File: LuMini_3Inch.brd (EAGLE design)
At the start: 76.2 x 76.2 mm, 97 parts, among them J1 SOLDER_PAD_2, J2 SOLDER_PAD_2, J3 SOLDER_PAD_2

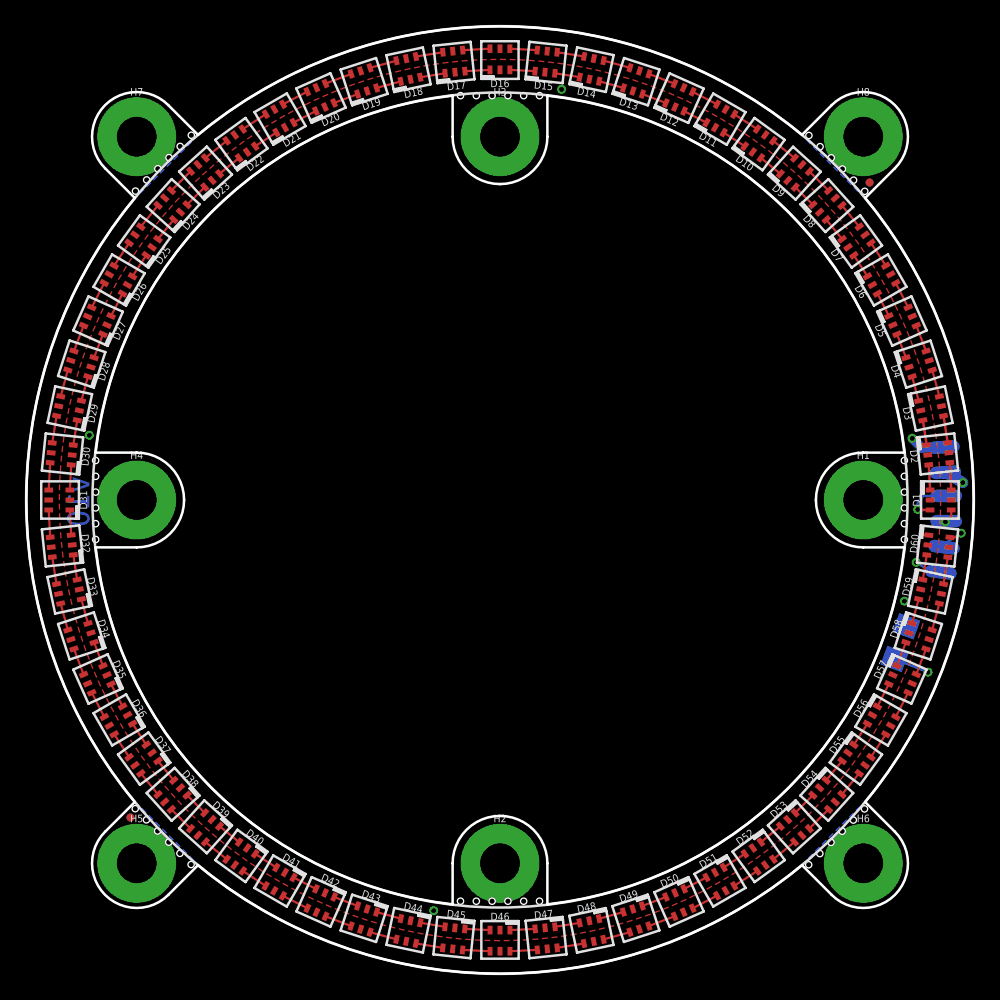
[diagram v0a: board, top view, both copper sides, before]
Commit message: added lumini ring
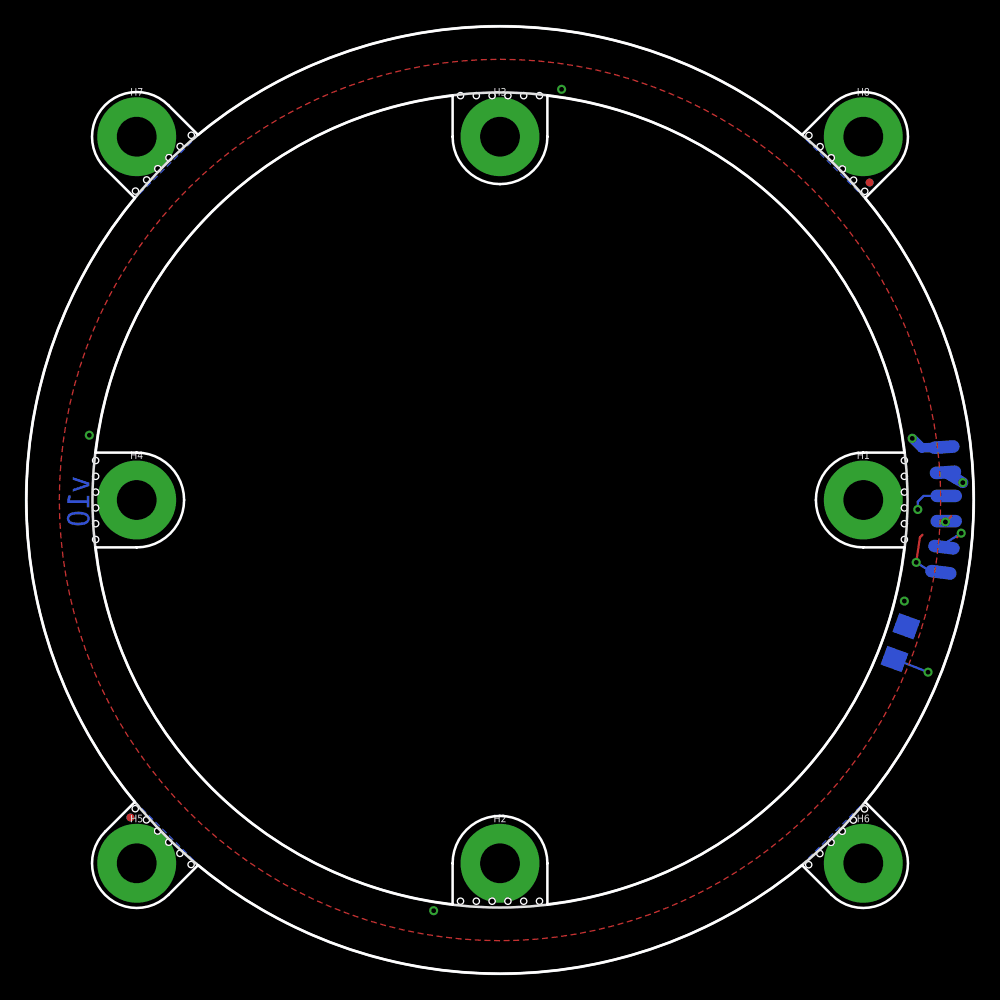
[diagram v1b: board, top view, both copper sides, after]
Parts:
- removed D1, D10, D11, D12, D13, D14, D15, D16, D17, D18, D19, D2, D20, D21, D22, D23, D24, D25, D26, D27, D28, D29, D3, D30, D31, D32, D33, D34, D35, D36, D37, D38, D39, D4, D40, D41, D42, D43, D44, D45, D46, D47, D48, D49, D5, D50, D51, D52, D53, D54, D55, D56, D57, D58, D59, D6, D60, D7, D8, D9: APA102-2020, SparkFun-LED:APA102-2020
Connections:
- removed net N$1: D4.CKO, D5.CKI
- removed net N$10: D4.SDO, D5.SDI
- removed net N$100: D50.CKO, D51.CKI
- removed net N$101: D50.SDO, D51.SDI
- removed net N$102: D51.CKO, D52.CKI
- removed net N$103: D51.SDO, D52.SDI
- removed net N$104: D52.CKO, D53.CKI
- removed net N$105: D52.SDO, D53.SDI
- removed net N$106: D53.CKO, D54.CKI
- removed net N$107: D53.SDO, D54.SDI
- removed net N$108: D54.CKO, D55.CKI
- removed net N$109: D54.SDO, D55.SDI
- removed net N$11: D5.CKO, D6.CKI
- removed net N$110: D55.CKO, D56.CKI
- removed net N$111: D55.SDO, D56.SDI
- removed net N$112: D57.CKO, D58.CKI
- removed net N$113: D57.SDO, D58.SDI
- removed net N$114: D58.SDO, D59.SDI
- removed net N$115: D59.CKO, D60.CKI
- removed net N$116: D59.SDO, D60.SDI
- removed net N$117: D58.CKO, D59.CKI
- removed net N$118: D48.CKO, D49.CKI
- removed net N$119: D48.SDO, D49.SDI
- removed net N$12: D5.SDO, D6.SDI
- removed net N$120: D56.SDO, D57.SDI
- removed net N$121: D56.CKO, D57.CKI
- removed net N$124: D20.CKO, D21.CKI
- removed net N$13: D6.CKO, D7.CKI
- removed net N$14: D6.SDO, D7.SDI
- removed net N$15: D7.CKO, D8.CKI
- removed net N$16: D7.SDO, D8.SDI
- removed net N$17: D16.SDO, D17.SDI
- removed net N$18: D20.SDO, D21.SDI
- removed net N$19: D10.CKI, D9.CKO
- removed net N$20: D10.SDI, D9.SDO
- removed net N$21: D10.CKO, D11.CKI
- removed net N$22: D10.SDO, D11.SDI
- removed net N$23: D11.CKO, D12.CKI
- removed net N$24: D11.SDO, D12.SDI
- removed net N$25: D12.CKO, D13.CKI
- removed net N$26: D12.SDO, D13.SDI
- removed net N$27: D13.CKO, D14.CKI
- removed net N$28: D13.SDO, D14.SDI
- removed net N$29: D14.CKO, D15.CKI
- removed net N$30: D14.SDO, D15.SDI
- removed net N$31: D45.CKO, D46.CKI
- removed net N$32: D30.CKO, D31.CKI
- removed net N$33: D8.CKO, D9.CKI
- removed net N$34: D8.SDO, D9.SDI
- removed net N$35: D17.CKO, D18.CKI
- removed net N$36: D17.SDO, D18.SDI
- removed net N$37: D18.CKO, D19.CKI
- removed net N$38: D18.SDO, D19.SDI
- removed net N$39: D19.CKO, D20.CKI
- removed net N$4: D1.CKO, D2.CKI
- removed net N$40: D19.SDO, D20.SDI
- removed net N$41: D30.SDO, D31.SDI
- removed net N$42: D15.CKO, D16.CKI
- removed net N$43: D16.CKO, D17.CKI
- removed net N$44: D21.CKO, D22.CKI
- removed net N$45: D21.SDO, D22.SDI
- removed net N$46: D22.CKO, D23.CKI
- removed net N$47: D22.SDO, D23.SDI
- removed net N$48: D23.CKO, D24.CKI
- removed net N$49: D23.SDO, D24.SDI
- removed net N$5: D1.SDO, D2.SDI
- removed net N$50: D24.CKO, D25.CKI
- removed net N$51: D24.SDO, D25.SDI
- removed net N$52: D25.CKO, D26.CKI
- removed net N$53: D25.SDO, D26.SDI
- removed net N$54: D26.CKO, D27.CKI
- removed net N$55: D26.SDO, D27.SDI
- removed net N$56: D27.CKO, D28.CKI
- removed net N$57: D27.SDO, D28.SDI
- removed net N$58: D29.CKO, D30.CKI
- removed net N$59: D29.SDO, D30.SDI
- removed net N$6: D2.CKO, D3.CKI
- removed net N$60: D15.SDO, D16.SDI
- removed net N$61: D45.SDO, D46.SDI
- removed net N$62: D31.CKO, D32.CKI
- removed net N$63: D31.SDO, D32.SDI
- removed net N$64: D32.CKO, D33.CKI
- removed net N$65: D32.SDO, D33.SDI
- removed net N$66: D33.CKO, D34.CKI
- removed net N$67: D33.SDO, D34.SDI
- removed net N$68: D34.CKO, D35.CKI
- removed net N$69: D34.SDO, D35.SDI
- removed net N$7: D2.SDO, D3.SDI
- removed net N$70: D35.CKO, D36.CKI
- removed net N$71: D35.SDO, D36.SDI
- removed net N$72: D37.CKO, D38.CKI
- removed net N$73: D37.SDO, D38.SDI
- removed net N$74: D38.SDO, D39.SDI
- removed net N$75: D39.CKO, D40.CKI
- removed net N$76: D39.SDO, D40.SDI
- removed net N$77: D38.CKO, D39.CKI
- removed net N$78: D28.CKO, D29.CKI
- removed net N$79: D28.SDO, D29.SDI
- removed net N$8: D3.CKO, D4.CKI
- removed net N$80: D36.SDO, D37.SDI
- removed net N$81: D36.CKO, D37.CKI
- removed net N$82: D40.CKO, D41.CKI
- removed net N$83: D40.SDO, D41.SDI
- removed net N$84: D41.CKO, D42.CKI
- removed net N$85: D41.SDO, D42.SDI
- removed net N$86: D42.CKO, D43.CKI
- removed net N$87: D42.SDO, D43.SDI
- removed net N$88: D43.CKO, D44.CKI
- removed net N$89: D43.SDO, D44.SDI
- removed net N$9: D3.SDO, D4.SDI
- removed net N$90: D44.CKO, D45.CKI
- removed net N$91: D44.SDO, D45.SDI
- removed net N$94: D46.CKO, D47.CKI
- removed net N$95: D46.SDO, D47.SDI
- removed net N$96: D47.CKO, D48.CKI
- removed net N$97: D47.SDO, D48.SDI
- removed net N$98: D49.CKO, D50.CKI
- removed net N$99: D49.SDO, D50.SDI
- net 5V: no longer D1.VDD, D10.VDD, D11.VDD, D12.VDD, D13.VDD, D14.VDD, D15.VDD, D16.VDD, D17.VDD, D18.VDD, D19.VDD, D2.VDD, D20.VDD, D21.VDD, D22.VDD, D23.VDD, D24.VDD, D25.VDD, D26.VDD, D27.VDD, D28.VDD, D29.VDD, D3.VDD, D30.VDD, D31.VDD, D32.VDD, D33.VDD, D34.VDD, D35.VDD, D36.VDD, D37.VDD, D38.VDD, D39.VDD, D4.VDD, D40.VDD, D41.VDD, D42.VDD, D43.VDD, D44.VDD, D45.VDD, D46.VDD, D47.VDD, D48.VDD, D49.VDD, D5.VDD, D50.VDD, D51.VDD, D52.VDD, D53.VDD, D54.VDD, D55.VDD, D56.VDD, D57.VDD, D58.VDD, D59.VDD, D6.VDD, D60.VDD, D7.VDD, D8.VDD, D9.VDD
- net CI: no longer D1.CKI
- net CO: no longer D60.CKO
- net DI: no longer D1.SDI
- net DO: no longer D60.SDO
- net GND: no longer D1.GND, D10.GND, D11.GND, D12.GND, D13.GND, D14.GND, D15.GND, D16.GND, D17.GND, D18.GND, D19.GND, D2.GND, D20.GND, D21.GND, D22.GND, D23.GND, D24.GND, D25.GND, D26.GND, D27.GND, D28.GND, D29.GND, D3.GND, D30.GND, D31.GND, D32.GND, D33.GND, D34.GND, D35.GND, D36.GND, D37.GND, D38.GND, D39.GND, D4.GND, D40.GND, D41.GND, D42.GND, D43.GND, D44.GND, D45.GND, D46.GND, D47.GND, D48.GND, D49.GND, D5.GND, D50.GND, D51.GND, D52.GND, D53.GND, D54.GND, D55.GND, D56.GND, D57.GND, D58.GND, D59.GND, D6.GND, D60.GND, D7.GND, D8.GND, D9.GND
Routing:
- net N$98: track 2.21 -> 0.00 mm
- net N$15: track 2.21 -> 0.00 mm
- net N$75: track 2.21 -> 0.00 mm
- net N$31: track 2.21 -> 0.00 mm
- net N$50: track 2.21 -> 0.00 mm
- net N$4: track 2.21 -> 0.00 mm
- net N$42: track 2.21 -> 0.00 mm
- net N$94: track 2.21 -> 0.00 mm
- net N$39: track 2.21 -> 0.00 mm
- net N$1: track 2.21 -> 0.00 mm
- net N$44: track 2.21 -> 0.00 mm
- net N$117: track 2.21 -> 0.00 mm
- net N$54: track 2.21 -> 0.00 mm
- net N$19: track 2.21 -> 0.00 mm
- net N$108: track 2.21 -> 0.00 mm
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
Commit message: about to repin IVL
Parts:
- added D1, D10, D11, D12, D13, D14, D15, D16, D17, D18, D19, D2, D20, D21, D22, D23, D24, D25, D26, D27, D28, D29, D3, D30, D31, D32, D33, D34, D35, D36, D37, D38, D39, D4, D40, D41, D42, D43, D44, D45, D46, D47, D48, D49, D5, D50, D51, D52, D53, D54, D55, D56, D57, D58, D59, D6, D60, D7, D8, D9: APA102-2020, SparkFun-LED:APA102-2020
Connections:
- new net N$1: D4.CKO, D5.CKI
- new net N$10: D4.SDO, D5.SDI
- new net N$100: D50.CKO, D51.CKI
- new net N$101: D50.SDO, D51.SDI
- new net N$102: D51.CKO, D52.CKI
- new net N$103: D51.SDO, D52.SDI
- new net N$104: D52.CKO, D53.CKI
- new net N$105: D52.SDO, D53.SDI
- new net N$106: D53.CKO, D54.CKI
- new net N$107: D53.SDO, D54.SDI
- new net N$108: D54.CKO, D55.CKI
- new net N$109: D54.SDO, D55.SDI
- new net N$11: D5.CKO, D6.CKI
- new net N$110: D55.CKO, D56.CKI
- new net N$111: D55.SDO, D56.SDI
- new net N$112: D57.CKO, D58.CKI
- new net N$113: D57.SDO, D58.SDI
- new net N$114: D58.SDO, D59.SDI
- new net N$115: D59.CKO, D60.CKI
- new net N$116: D59.SDO, D60.SDI
- new net N$117: D58.CKO, D59.CKI
- new net N$118: D48.CKO, D49.CKI
- new net N$119: D48.SDO, D49.SDI
- new net N$12: D5.SDO, D6.SDI
- new net N$120: D56.SDO, D57.SDI
- new net N$121: D56.CKO, D57.CKI
- new net N$124: D20.CKO, D21.CKI
- new net N$13: D6.CKO, D7.CKI
- new net N$14: D6.SDO, D7.SDI
- new net N$15: D7.CKO, D8.CKI
- new net N$16: D7.SDO, D8.SDI
- new net N$17: D16.SDO, D17.SDI
- new net N$18: D20.SDO, D21.SDI
- new net N$19: D10.CKI, D9.CKO
- new net N$20: D10.SDI, D9.SDO
- new net N$21: D10.CKO, D11.CKI
- new net N$22: D10.SDO, D11.SDI
- new net N$23: D11.CKO, D12.CKI
- new net N$24: D11.SDO, D12.SDI
- new net N$25: D12.CKO, D13.CKI
- new net N$26: D12.SDO, D13.SDI
- new net N$27: D13.CKO, D14.CKI
- new net N$28: D13.SDO, D14.SDI
- new net N$29: D14.CKO, D15.CKI
- new net N$30: D14.SDO, D15.SDI
- new net N$31: D45.CKO, D46.CKI
- new net N$32: D30.CKO, D31.CKI
- new net N$33: D8.CKO, D9.CKI
- new net N$34: D8.SDO, D9.SDI
- new net N$35: D17.CKO, D18.CKI
- new net N$36: D17.SDO, D18.SDI
- new net N$37: D18.CKO, D19.CKI
- new net N$38: D18.SDO, D19.SDI
- new net N$39: D19.CKO, D20.CKI
- new net N$4: D1.CKO, D2.CKI
- new net N$40: D19.SDO, D20.SDI
- new net N$41: D30.SDO, D31.SDI
- new net N$42: D15.CKO, D16.CKI
- new net N$43: D16.CKO, D17.CKI
- new net N$44: D21.CKO, D22.CKI
- new net N$45: D21.SDO, D22.SDI
- new net N$46: D22.CKO, D23.CKI
- new net N$47: D22.SDO, D23.SDI
- new net N$48: D23.CKO, D24.CKI
- new net N$49: D23.SDO, D24.SDI
- new net N$5: D1.SDO, D2.SDI
- new net N$50: D24.CKO, D25.CKI
- new net N$51: D24.SDO, D25.SDI
- new net N$52: D25.CKO, D26.CKI
- new net N$53: D25.SDO, D26.SDI
- new net N$54: D26.CKO, D27.CKI
- new net N$55: D26.SDO, D27.SDI
- new net N$56: D27.CKO, D28.CKI
- new net N$57: D27.SDO, D28.SDI
- new net N$58: D29.CKO, D30.CKI
- new net N$59: D29.SDO, D30.SDI
- new net N$6: D2.CKO, D3.CKI
- new net N$60: D15.SDO, D16.SDI
- new net N$61: D45.SDO, D46.SDI
- new net N$62: D31.CKO, D32.CKI
- new net N$63: D31.SDO, D32.SDI
- new net N$64: D32.CKO, D33.CKI
- new net N$65: D32.SDO, D33.SDI
- new net N$66: D33.CKO, D34.CKI
- new net N$67: D33.SDO, D34.SDI
- new net N$68: D34.CKO, D35.CKI
- new net N$69: D34.SDO, D35.SDI
- new net N$7: D2.SDO, D3.SDI
- new net N$70: D35.CKO, D36.CKI
- new net N$71: D35.SDO, D36.SDI
- new net N$72: D37.CKO, D38.CKI
- new net N$73: D37.SDO, D38.SDI
- new net N$74: D38.SDO, D39.SDI
- new net N$75: D39.CKO, D40.CKI
- new net N$76: D39.SDO, D40.SDI
- new net N$77: D38.CKO, D39.CKI
- new net N$78: D28.CKO, D29.CKI
- new net N$79: D28.SDO, D29.SDI
- new net N$8: D3.CKO, D4.CKI
- new net N$80: D36.SDO, D37.SDI
- new net N$81: D36.CKO, D37.CKI
- new net N$82: D40.CKO, D41.CKI
- new net N$83: D40.SDO, D41.SDI
- new net N$84: D41.CKO, D42.CKI
- new net N$85: D41.SDO, D42.SDI
- new net N$86: D42.CKO, D43.CKI
- new net N$87: D42.SDO, D43.SDI
- new net N$88: D43.CKO, D44.CKI
- new net N$89: D43.SDO, D44.SDI
- new net N$9: D3.SDO, D4.SDI
- new net N$90: D44.CKO, D45.CKI
- new net N$91: D44.SDO, D45.SDI
- new net N$94: D46.CKO, D47.CKI
- new net N$95: D46.SDO, D47.SDI
- new net N$96: D47.CKO, D48.CKI
- new net N$97: D47.SDO, D48.SDI
- new net N$98: D49.CKO, D50.CKI
- new net N$99: D49.SDO, D50.SDI
- net 5V: now also D1.VDD, D10.VDD, D11.VDD, D12.VDD, D13.VDD, D14.VDD, D15.VDD, D16.VDD, D17.VDD, D18.VDD, D19.VDD, D2.VDD, D20.VDD, D21.VDD, D22.VDD, D23.VDD, D24.VDD, D25.VDD, D26.VDD, D27.VDD, D28.VDD, D29.VDD, D3.VDD, D30.VDD, D31.VDD, D32.VDD, D33.VDD, D34.VDD, D35.VDD, D36.VDD, D37.VDD, D38.VDD, D39.VDD, D4.VDD, D40.VDD, D41.VDD, D42.VDD, D43.VDD, D44.VDD, D45.VDD, D46.VDD, D47.VDD, D48.VDD, D49.VDD, D5.VDD, D50.VDD, D51.VDD, D52.VDD, D53.VDD, D54.VDD, D55.VDD, D56.VDD, D57.VDD, D58.VDD, D59.VDD, D6.VDD, D60.VDD, D7.VDD, D8.VDD, D9.VDD
- net CI: now also D1.CKI
- net CO: now also D60.CKO
- net DI: now also D1.SDI
- net DO: now also D60.SDO
- net GND: now also D1.GND, D10.GND, D11.GND, D12.GND, D13.GND, D14.GND, D15.GND, D16.GND, D17.GND, D18.GND, D19.GND, D2.GND, D20.GND, D21.GND, D22.GND, D23.GND, D24.GND, D25.GND, D26.GND, D27.GND, D28.GND, D29.GND, D3.GND, D30.GND, D31.GND, D32.GND, D33.GND, D34.GND, D35.GND, D36.GND, D37.GND, D38.GND, D39.GND, D4.GND, D40.GND, D41.GND, D42.GND, D43.GND, D44.GND, D45.GND, D46.GND, D47.GND, D48.GND, D49.GND, D5.GND, D50.GND, D51.GND, D52.GND, D53.GND, D54.GND, D55.GND, D56.GND, D57.GND, D58.GND, D59.GND, D6.GND, D60.GND, D7.GND, D8.GND, D9.GND
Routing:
- net N$98: track 0.00 -> 2.21 mm
- net N$15: track 0.00 -> 2.21 mm
- net N$75: track 0.00 -> 2.21 mm
- net N$31: track 0.00 -> 2.21 mm
- net N$50: track 0.00 -> 2.21 mm
- net N$4: track 0.00 -> 2.21 mm
- net N$42: track 0.00 -> 2.21 mm
- net N$94: track 0.00 -> 2.21 mm
- net N$39: track 0.00 -> 2.21 mm
- net N$1: track 0.00 -> 2.21 mm
- net N$44: track 0.00 -> 2.21 mm
- net N$117: track 0.00 -> 2.21 mm
- net N$54: track 0.00 -> 2.21 mm
- net N$19: track 0.00 -> 2.21 mm
- net N$108: track 0.00 -> 2.21 mm
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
